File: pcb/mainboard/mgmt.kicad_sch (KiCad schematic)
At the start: 102 parts, among them J10 FAN_01, J11 XILINX_JTAG, J12 JUMPER_0402_SPDT, J13 JUMPER_0402_SPDT, J14 RJ45, J15 PMOD_HOST, J48 CONN_01X10, J8 FAN_01, J9 CONN_01X03, U23 STM32H735-UFBGA176-25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

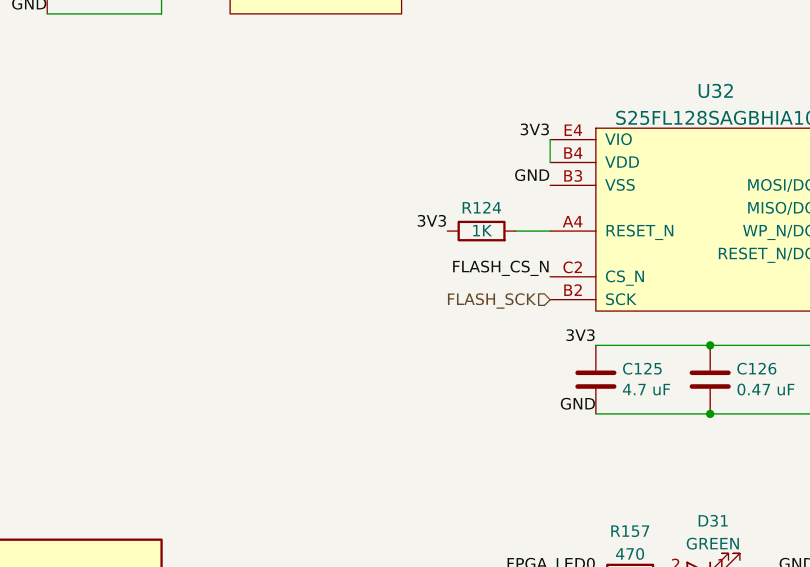
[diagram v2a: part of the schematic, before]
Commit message: Initial FPGA routing
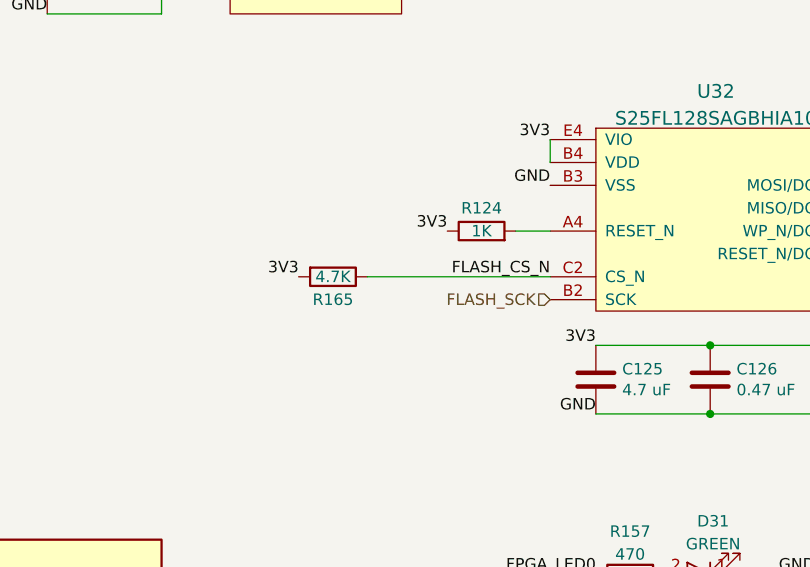
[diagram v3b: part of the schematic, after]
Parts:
- added R165: 4.7K, azonenberg_pcb:EIA_0402_RES_NOSILK, symbol device:R
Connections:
- net 3V3: now also R165.2
- net FLASH_CS_N: now also R165.1
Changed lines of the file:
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@@
   (title_block
     (title "Trigger Crossbar")
-    (date "2023-12-20")
+    (date "2023-12-22")
     (rev "0.1")
     (company "Antikernel Labs")
@@
     (stroke (width 0) (type default) (color 0 0 0 0))
   )
+  (wire (pts (xy 264.16 167.64) (xy 284.48 167.64))
+    (stroke (width 0) (type default) (color 0 0 0 0))
+  )
   (wire (pts (xy 153.67 245.11) (xy 161.29 245.11))
     (stroke (width 0) (type default) (color 0 0 0 0))
@@
     (effects (font (size 1.27 1.27)) (justify right bottom))
   )
+  (label "3V3" (at 256.54 167.64 180)
+    (effects (font (size 1.27 1.27)) (justify right bottom))
+  )
   (label "GND" (at 284.48 157.48 180)
     (effects (font (size 1.27 1.27)) (justify right bottom))
@@
     (pin "M3")
   )
+  (symbol (lib_id "device:R") (at 260.35 167.64 270) (unit 1)
+    (in_bom yes) (on_board yes)
+    (property "Reference" "R165" (id 0) (at 260.35 170.18 90))
+    (property "Value" "4.7K" (id 1) (at 260.35 167.64 90))
+    (property "Footprint" "azonenberg_pcb:EIA_0402_RES_NOSILK" (id 2) (at 260.35 165.862 90)
+      (effects (font (size 1.27 1.27)) hide)
+    )
+    (property "Datasheet" "" (id 3) (at 260.35 167.64 0)
+      (effects (font (size 1.27 1.27)) hide)
+    )
+    (pin "1")
+    (pin "2")
+  )
   (symbol (lib_id "special-azonenberg:ADM3101E_QFN") (at 147.32 229.87 0) (unit 1)

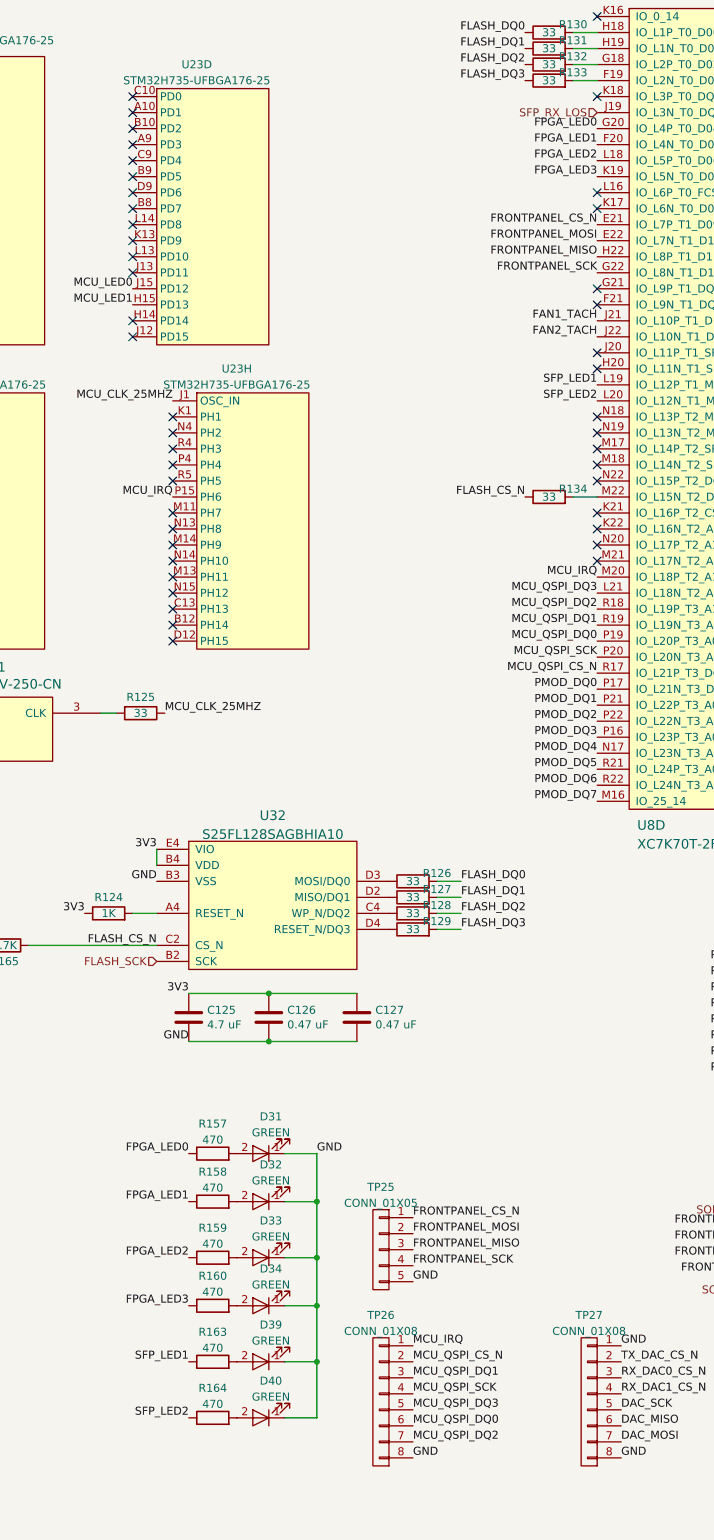
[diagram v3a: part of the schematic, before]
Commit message: Hooked up most input pins
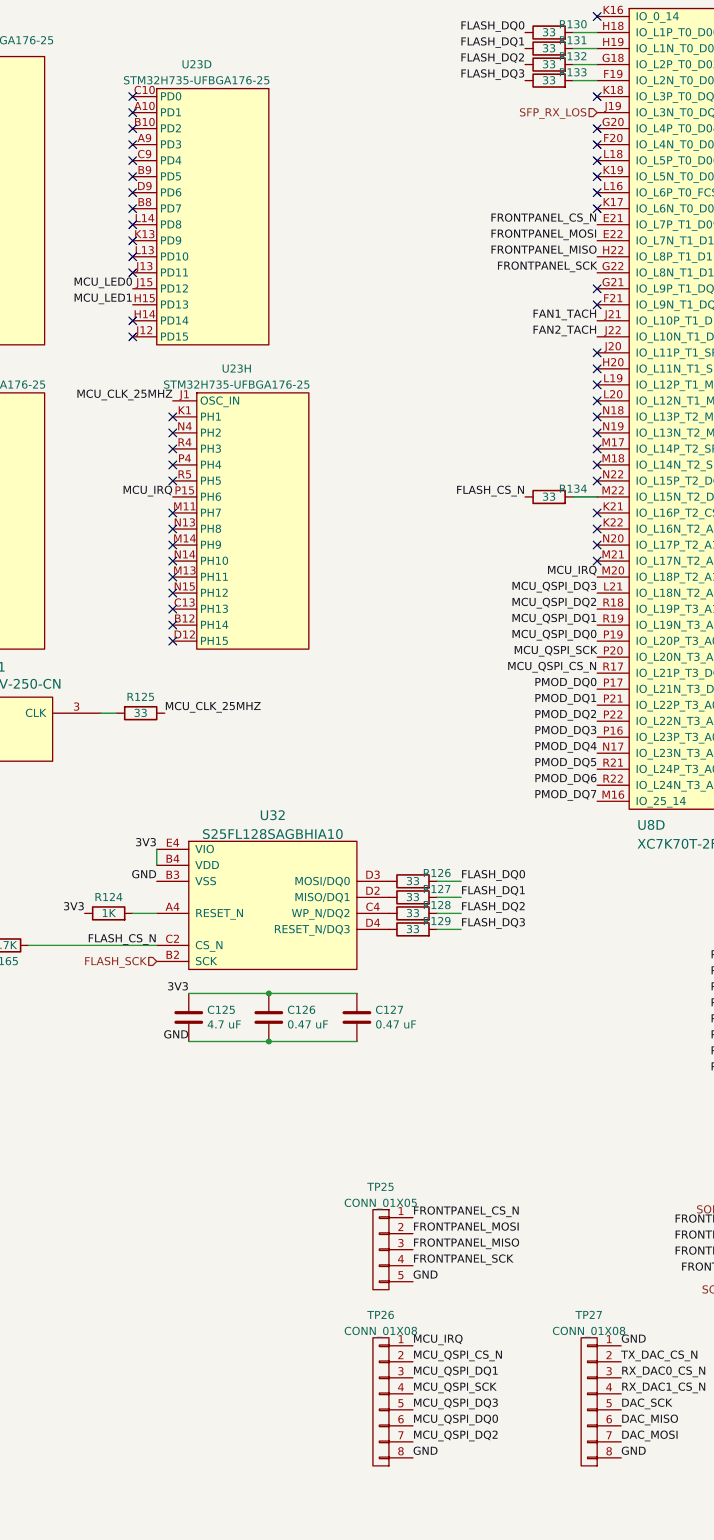
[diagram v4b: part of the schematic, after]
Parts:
- removed D31, D32, D33, D34, D39, D40: GREEN, azonenberg_pcb:EIA_0603_LED, symbol device:LED
- removed R157, R158, R159, R160, R163, R164: 470, azonenberg_pcb:EIA_0402_RES_NOSILK, symbol device:R
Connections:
- net FPGA_LED0: no longer names the net of U8.G20 (IO_L4P_T0_D04_14)
- net FPGA_LED1: no longer names the net of U8.F20 (IO_L4N_T0_D05_14)
- net FPGA_LED2: no longer names the net of U8.L18 (IO_L5P_T0_D06_14)
- net FPGA_LED3: no longer names the net of U8.K19 (IO_L5N_T0_D07_14)
- net SFP_LED1: no longer names the net of U8.L19 (IO_L12P_T1_MRCC_14)
- net SFP_LED2: no longer names the net of U8.L20 (IO_L12N_T1_MRCC_14)
- no-connect marks 114 -> 120

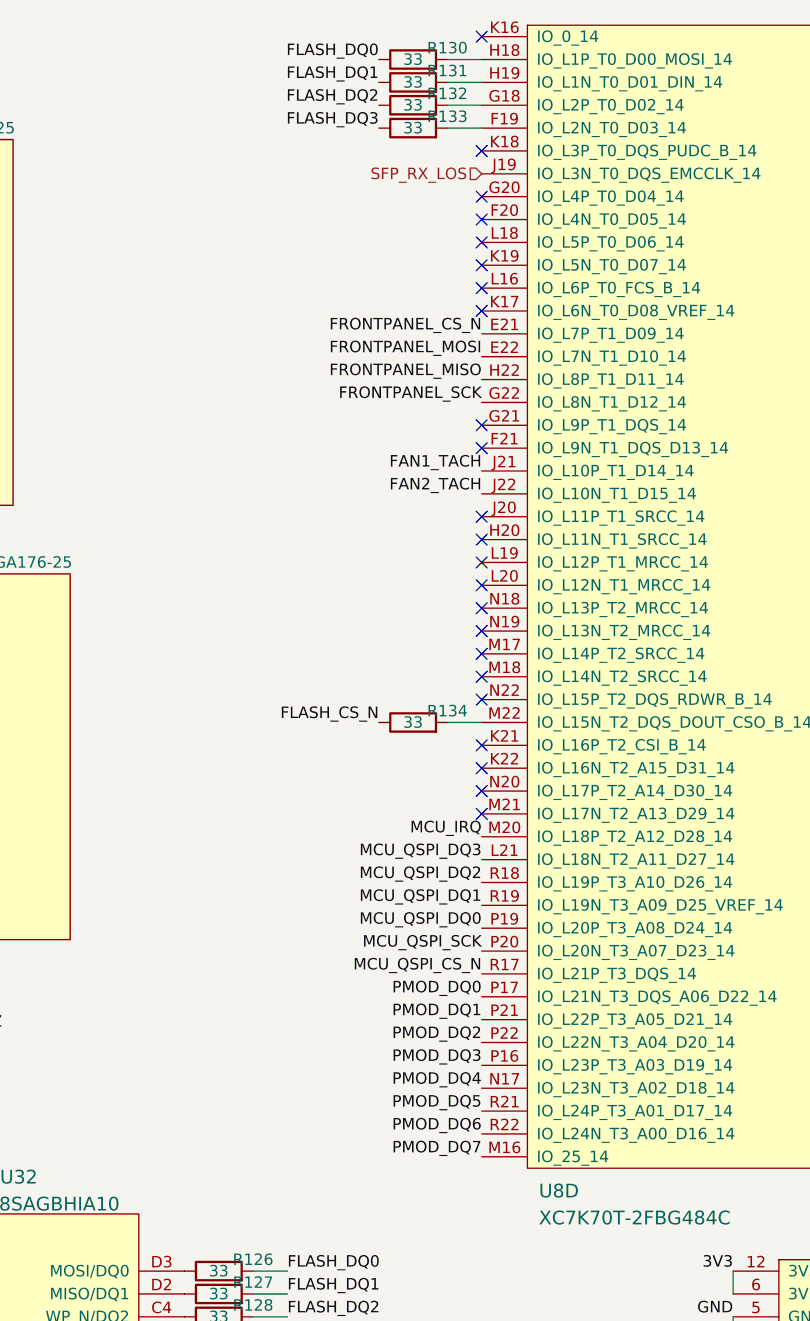
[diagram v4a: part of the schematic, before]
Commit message: Hooked up PMOD, initial placement of FPGA JTAG
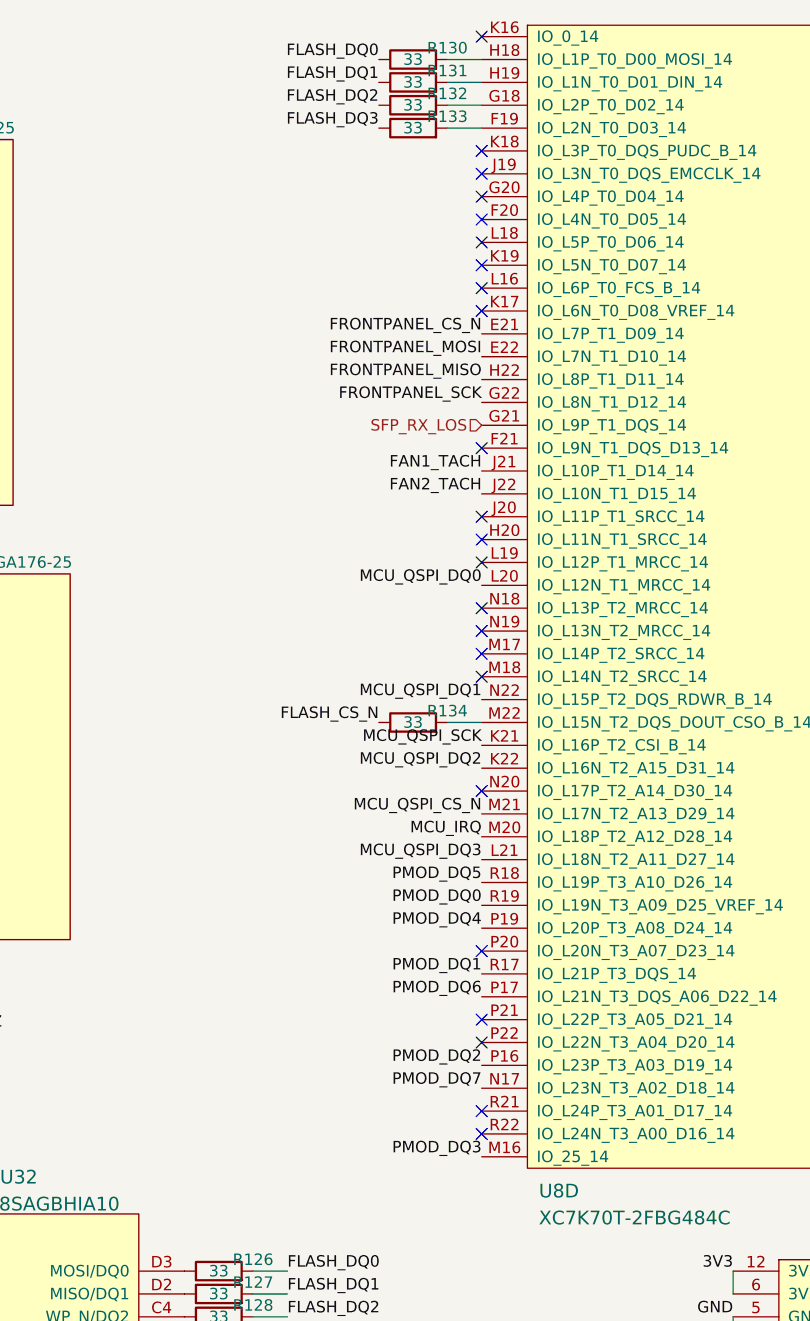
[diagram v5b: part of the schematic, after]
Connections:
- net MCU_QSPI_CS_N: now also U8.M21 (IO_L17N_T2_A13_D29_14); no longer U8.R17 (IO_L21P_T3_DQS_14)
- net MCU_QSPI_DQ0: now also U8.L20 (IO_L12N_T1_MRCC_14); no longer U8.P19 (IO_L20P_T3_A08_D24_14)
- net MCU_QSPI_DQ1: now also U8.N22 (IO_L15P_T2_DQS_RDWR_B_14); no longer U8.R19 (IO_L19N_T3_A09_D25_VREF_14)
- net MCU_QSPI_DQ2: now also U8.K22 (IO_L16N_T2_A15_D31_14); no longer U8.R18 (IO_L19P_T3_A10_D26_14)
- net MCU_QSPI_SCK: now also U8.K21 (IO_L16P_T2_CSI_B_14); no longer U8.P20 (IO_L20N_T3_A07_D23_14)
- net PMOD_DQ0: now also U8.R19 (IO_L19N_T3_A09_D25_VREF_14); no longer U8.P17 (IO_L21N_T3_DQS_A06_D22_14)
- net PMOD_DQ1: now also U8.R17 (IO_L21P_T3_DQS_14); no longer U8.P21 (IO_L22P_T3_A05_D21_14)
- net PMOD_DQ2: now also U8.P16 (IO_L23P_T3_A03_D19_14); no longer U8.P22 (IO_L22N_T3_A04_D20_14)
- net PMOD_DQ3: now also U8.M16 (IO_25_14); no longer U8.P16 (IO_L23P_T3_A03_D19_14)
- net PMOD_DQ4: now also U8.P19 (IO_L20P_T3_A08_D24_14); no longer U8.N17 (IO_L23N_T3_A02_D18_14)
- net PMOD_DQ5: now also U8.R18 (IO_L19P_T3_A10_D26_14); no longer U8.R21 (IO_L24P_T3_A01_D17_14)
- net PMOD_DQ6: now also U8.P17 (IO_L21N_T3_DQS_A06_D22_14); no longer U8.R22 (IO_L24N_T3_A00_D16_14)
- net PMOD_DQ7: now also U8.N17 (IO_L23N_T3_A02_D18_14); no longer U8.M16 (IO_25_14)
- net SFP_RX_LOS: now also U8.G21 (IO_L9P_T1_DQS_14); no longer U8.J19 (IO_L3N_T0_DQS_EMCCLK_14)
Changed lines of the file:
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@@
   (no_connect (at 245.11 60.96))
   (no_connect (at 287.02 91.44))
-  (no_connect (at 354.33 81.28))
   (no_connect (at 280.67 71.12))
   (no_connect (at 354.33 40.64))
@@
   (no_connect (at 93.98 167.64))
   (no_connect (at 245.11 53.34))
+  (no_connect (at 354.33 35.56))
   (no_connect (at 354.33 78.74))
   (no_connect (at 200.66 106.68))
@@
   (no_connect (at 245.11 116.84))
   (no_connect (at 152.4 27.94))
-  (no_connect (at 354.33 63.5))
-  (no_connect (at 354.33 101.6))
   (no_connect (at 245.11 111.76))
   (no_connect (at 280.67 43.18))
@@
   (no_connect (at 152.4 101.6))
   (no_connect (at 287.02 86.36))
+  (no_connect (at 354.33 121.92))
   (no_connect (at 152.4 30.48))
   (no_connect (at 200.66 50.8))
@@
   (no_connect (at 354.33 91.44))
   (no_connect (at 200.66 116.84))
+  (no_connect (at 354.33 139.7))
   (no_connect (at 200.66 111.76))
   (no_connect (at 280.67 50.8))
@@
   (no_connect (at 200.66 93.98))
   (no_connect (at 245.11 35.56))
-  (no_connect (at 354.33 93.98))
   (no_connect (at 93.98 154.94))
   (no_connect (at 200.66 109.22))
@@
   (no_connect (at 152.4 58.42))
   (no_connect (at 245.11 101.6))
+  (no_connect (at 354.33 45.72))
   (no_connect (at 200.66 104.14))
   (no_connect (at 245.11 83.82))
@@
   (no_connect (at 287.02 99.06))
   (no_connect (at 280.67 38.1))
+  (no_connect (at 354.33 132.08))
   (no_connect (at 245.11 40.64))
   (no_connect (at 245.11 99.06))
@@
   (no_connect (at 152.4 81.28))
   (no_connect (at 152.4 35.56))
+  (no_connect (at 354.33 129.54))
   (no_connect (at 200.66 48.26))
-  (no_connect (at 354.33 106.68))
   (no_connect (at 152.4 119.38))
   (no_connect (at 200.66 114.3))
-  (no_connect (at 354.33 45.72))
   (no_connect (at 200.66 45.72))
   (no_connect (at 354.33 33.02))
@@
   (no_connect (at 287.02 111.76))
   (no_connect (at 245.11 43.18))
+  (no_connect (at 354.33 142.24))
   (no_connect (at 218.44 200.66))
   (no_connect (at 280.67 68.58))
@@
   (no_connect (at 354.33 76.2))
   (no_connect (at 287.02 116.84))
-  (no_connect (at 354.33 99.06))
   (no_connect (at 287.02 114.3))
   (no_connect (at 354.33 50.8))
@@
     (effects (font (size 1.27 1.27)) (justify right bottom))
   )
-  (label "PMOD_DQ3" (at 354.33 134.62 180)
+  (label "PMOD_DQ3" (at 354.33 144.78 180)
     (effects (font (size 1.27 1.27)) (justify right bottom))
   )
@@
     (effects (font (size 1.27 1.27)) (justify right bottom))
   )
-  (label "PMOD_DQ6" (at 354.33 142.24 180)
+  (label "PMOD_DQ6" (at 354.33 127 180)
     (effects (font (size 1.27 1.27)) (justify right bottom))
   )
@@
     (effects (font (size 1.27 1.27)) (justify right bottom))
   )
-  (label "MCU_QSPI_SCK" (at 354.33 121.92 180)
+  (label "MCU_QSPI_SCK" (at 354.33 99.06 180)
     (effects (font (size 1.27 1.27)) (justify right bottom))
   )
@@
     (effects (font (size 1.27 1.27)) (justify right bottom))
   )
-  (label "MCU_QSPI_DQ1" (at 354.33 116.84 180)
+  (label "MCU_QSPI_DQ1" (at 354.33 93.98 180)
     (effects (font (size 1.27 1.27)) (justify right bottom))
   )
@@
     (effects (font (size 1.27 1.27)) (justify right bottom))
   )
-  (label "PMOD_DQ2" (at 354.33 132.08 180)
+  (label "PMOD_DQ2" (at 354.33 134.62 180)
     (effects (font (size 1.27 1.27)) (justify right bottom))
   )
@@
     (effects (font (size 1.27 1.27)) (justify left bottom))
   )
-  (label "MCU_QSPI_CS_N" (at 354.33 124.46 180)
+  (label "MCU_QSPI_CS_N" (at 354.33 106.68 180)
     (effects (font (size 1.27 1.27)) (justify right bottom))
   )
@@
     (effects (font (size 1.27 1.27)) (justify left bottom))
   )
-  (label "MCU_QSPI_DQ0" (at 354.33 119.38 180)
+  (label "MCU_QSPI_DQ0" (at 354.33 81.28 180)
     (effects (font (size 1.27 1.27)) (justify right bottom))
   )
@@
     (effects (font (size 1.27 1.27)) (justify right bottom))
   )
-  (label "PMOD_DQ5" (at 354.33 139.7 180)
+  (label "PMOD_DQ5" (at 354.33 114.3 180)
     (effects (font (size 1.27 1.27)) (justify right bottom))
   )
@@
     (effects (font (size 1.27 1.27)) (justify right bottom))
   )
-  (label "MCU_QSPI_DQ2" (at 354.33 114.3 180)
+  (label "MCU_QSPI_DQ2" (at 354.33 101.6 180)
     (effects (font (size 1.27 1.27)) (justify right bottom))
   )
@@
     (effects (font (size 1.27 1.27)) (justify right bottom))
   )
-  (label "PMOD_DQ0" (at 354.33 127 180)
+  (label "PMOD_DQ0" (at 354.33 116.84 180)
     (effects (font (size 1.27 1.27)) (justify right bottom))
   )
@@
     (effects (font (size 1.27 1.27)) (justify left bottom))
   )
-  (label "PMOD_DQ7" (at 354.33 144.78 180)
+  (label "PMOD_DQ7" (at 354.33 137.16 180)
     (effects (font (size 1.27 1.27)) (justify right bottom))
   )
@@
     (effects (font (size 1.27 1.27)) (justify right bottom))
   )
-  (label "PMOD_DQ4" (at 354.33 137.16 180)
+  (label "PMOD_DQ4" (at 354.33 119.38 180)
     (effects (font (size 1.27 1.27)) (justify right bottom))
   )
@@
     (effects (font (size 1.27 1.27)) (justify right bottom))
   )
-  (label "PMOD_DQ1" (at 354.33 129.54 180)
+  (label "PMOD_DQ1" (at 354.33 124.46 180)
     (effects (font (size 1.27 1.27)) (justify right bottom))
   )
@@
     (effects (font (size 1.27 1.27)) (justify right))
   )
-  (hierarchical_label "SFP_RX_LOS" (shape input) (at 354.33 35.56 180)
+  (hierarchical_label "SFP_RX_LOS" (shape input) (at 354.33 63.5 180)
     (effects (font (size 1.27 1.27)) (justify right))
   )
